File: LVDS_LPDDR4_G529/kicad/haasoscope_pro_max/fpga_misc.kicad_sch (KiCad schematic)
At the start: 1 part, among them U3 Ti90G529_Functions

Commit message: Aligned schematics, sort of
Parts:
- removed U3: Ti90G529_Functions, G529:BGA-529_23x23_19.0x19.0mm, symbol Ti90G529_Functions:Ti90G529_Functions
- added IC1: ADC12DL500ACF_Aligned, BGA256C100P16X16_1700X1700X331, symbol Aligned_Peripheral_Symbols:ADC12DL500ACF_Aligned
- added U3: Ti90G529_Functions, haasoscope_pro_adc_fpga_board:BGA-529_23x23_19.0x19.0mm, symbol Ti90G529_Functions:Ti90G529_Functions

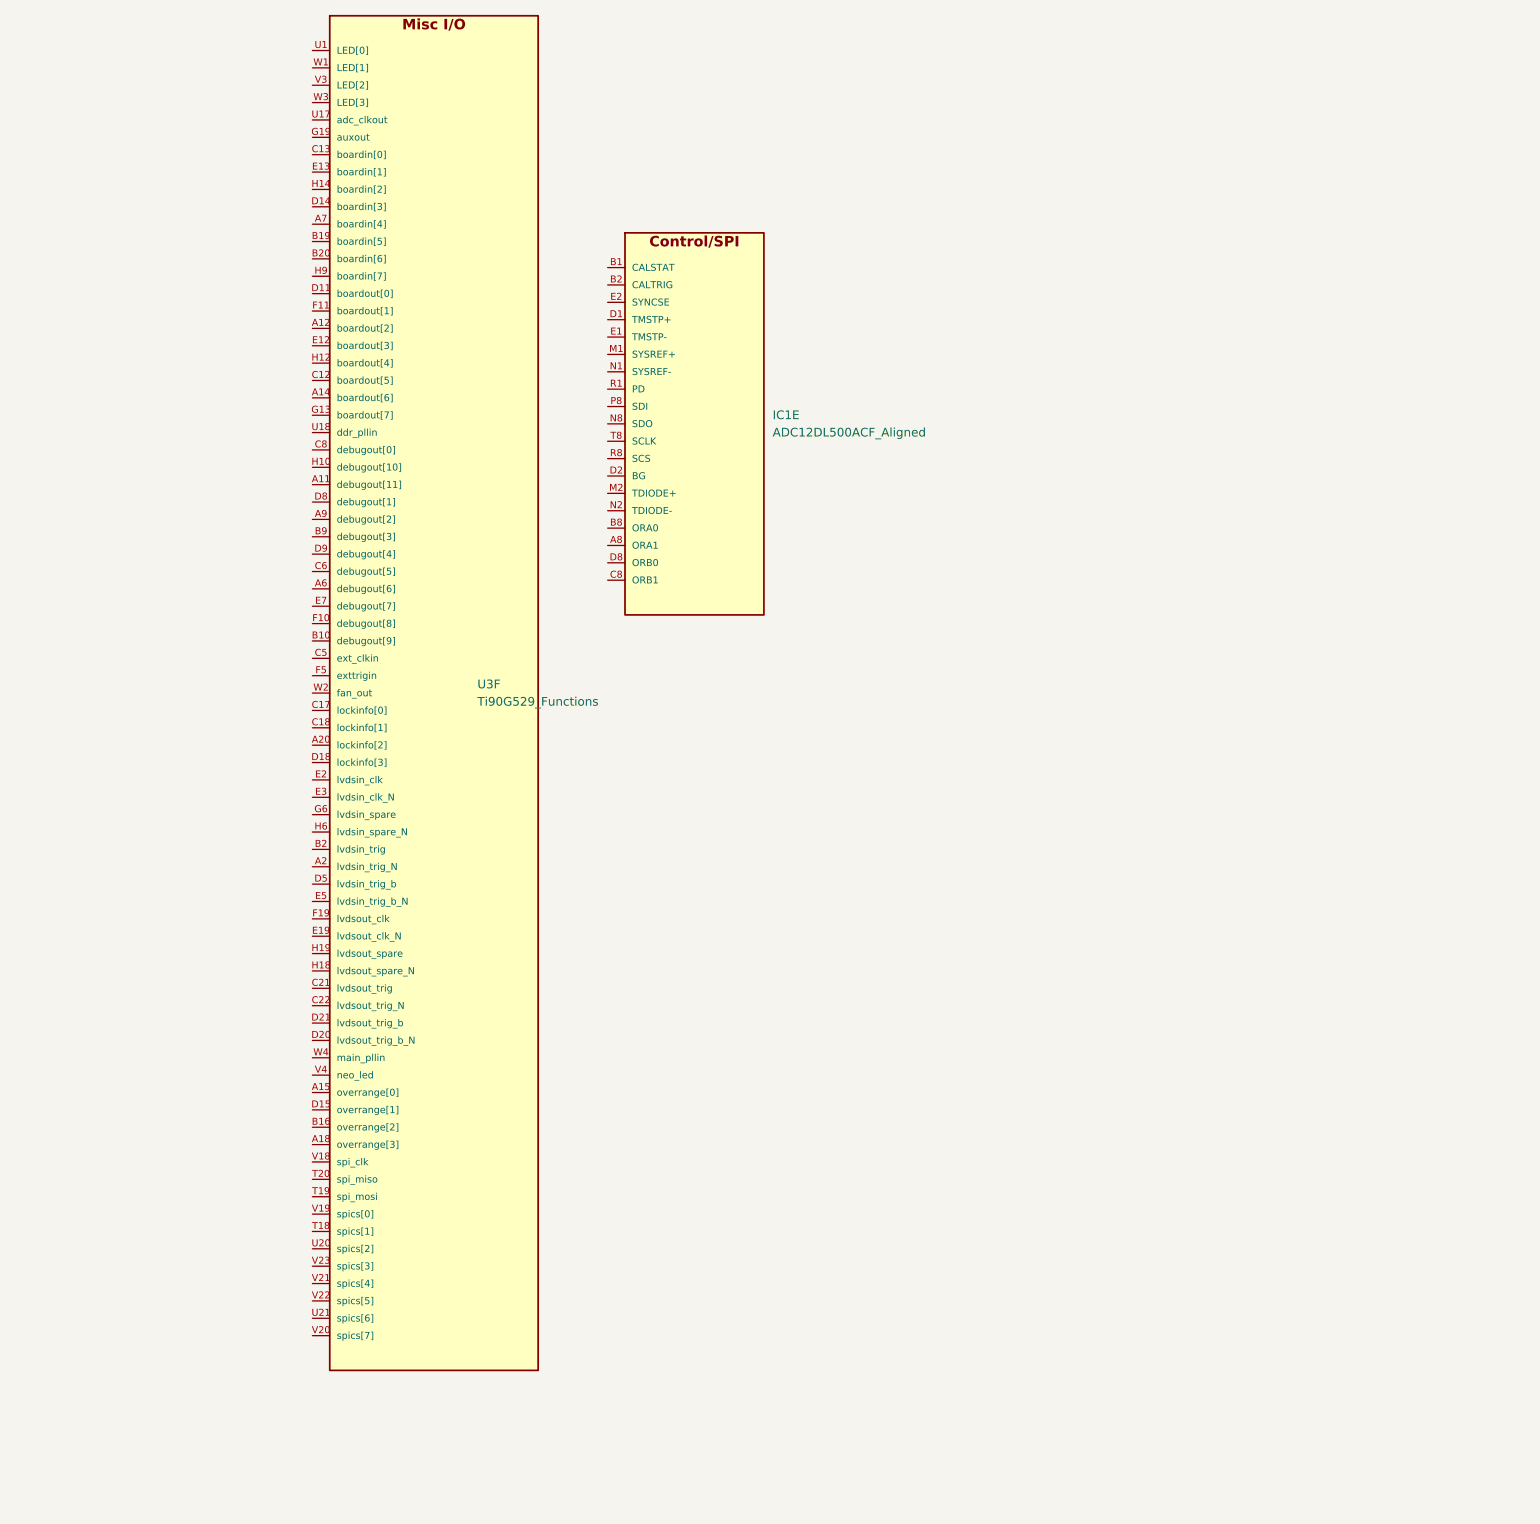
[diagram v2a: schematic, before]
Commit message: Aligned schematics, connected some components
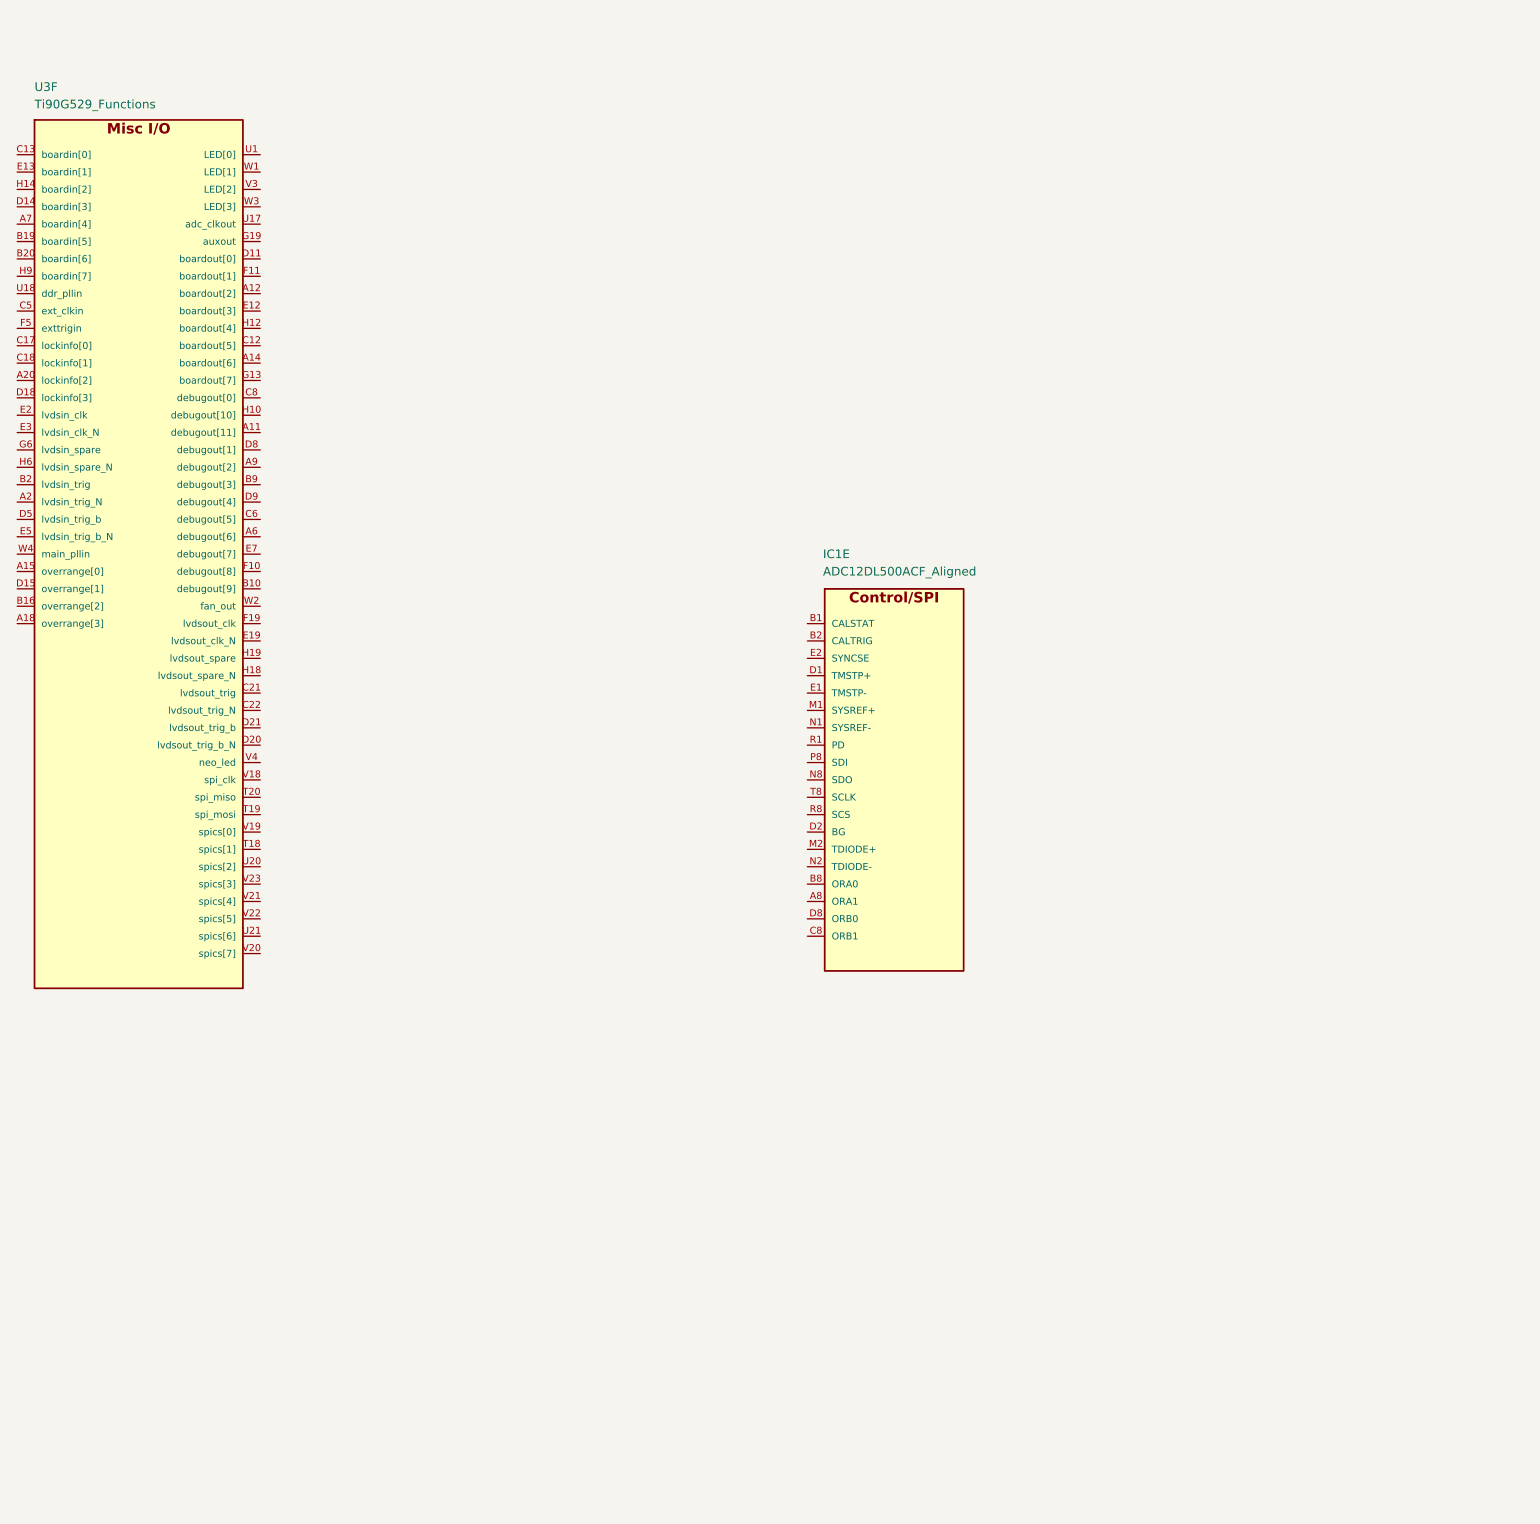
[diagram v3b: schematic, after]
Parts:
- IC1: footprint BGA256C100P16X16_1700X1700X331 -> ADC12DL:BGA256C100P16X16_1700X1700X331
- U3: footprint haasoscope_pro_adc_fpga_board:BGA-529_23x23_19.0x19.0mm -> G529:BGA-529_23x23_19.0x19.0mm
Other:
- moved on the sheet: IC1E, U3F
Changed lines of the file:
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@@
 	(symbol
 		(lib_id "Aligned_Peripheral_Symbols:ADC12DL500ACF_Aligned")
-		(at 152.4 77.47 0)
+		(at 181.61 129.54 0)
 		(unit 5)
 		(exclude_from_sim no)
@@
 		(on_board yes)
 		(dnp no)
-		(fields_autoplaced yes)
 		(property "Reference" "IC1"
-			(at 173.99 76.1852 0)
+			(at 181.356 96.52 0)
 			(effects
 				(font
@@
 		)
 		(property "Value" "ADC12DL500ACF_Aligned"
-			(at 173.99 78.7252 0)
+			(at 181.356 99.06 0)
 			(effects
 				(font
@@
 			)
 		)
-		(property "Footprint" "BGA256C100P16X16_1700X1700X331"
-			(at 152.4 81.28 0)
+		(property "Footprint" "ADC12DL:BGA256C100P16X16_1700X1700X331"
+			(at 181.61 133.35 0)
 			(effects
 				(font
@@
 		)
 		(property "Datasheet" ""
-			(at 152.4 77.47 0)
+			(at 181.61 129.54 0)
 			(effects
 				(font
@@
 		)
 		(property "Description" "ADC12DL500ACF - LVDS outputs aligned with Ti90G529 FPGA"
-			(at 152.4 83.82 0)
+			(at 181.61 135.89 0)
 			(effects
 				(font
@@
 	(symbol
 		(lib_id "Ti90G529_Functions:Ti90G529_Functions")
-		(at 109.22 116.84 0)
+		(at 66.04 96.52 0)
 		(unit 6)
 		(exclude_from_sim no)
@@
 		(on_board yes)
 		(dnp no)
-		(fields_autoplaced yes)
 		(property "Reference" "U3"
-			(at 130.81 115.5552 0)
+			(at 66.04 28.194 0)
 			(effects
 				(font
@@
 		)
 		(property "Value" "Ti90G529_Functions"
-			(at 130.81 118.0952 0)
+			(at 66.04 30.734 0)
 			(effects
 				(font
@@
 			)
 		)
-		(property "Footprint" "haasoscope_pro_adc_fpga_board:BGA-529_23x23_19.0x19.0mm"
-			(at 109.22 120.65 0)
+		(property "Footprint" "G529:BGA-529_23x23_19.0x19.0mm"
+			(at 66.04 100.33 0)
 			(effects
 				(font
@@
 		)
 		(property "Datasheet" ""
-			(at 109.22 123.19 0)
+			(at 66.04 102.87 0)
 			(effects
 				(font
@@
 		)
 		(property "Description" "Efinix Ti90G529 FPGA organized by peripheral interface"
-			(at 109.22 125.73 0)
-			(effects
-				(font
+			(at 66.04 105.41 0)
+			(effects
+				(font
